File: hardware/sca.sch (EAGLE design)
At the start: 31 parts

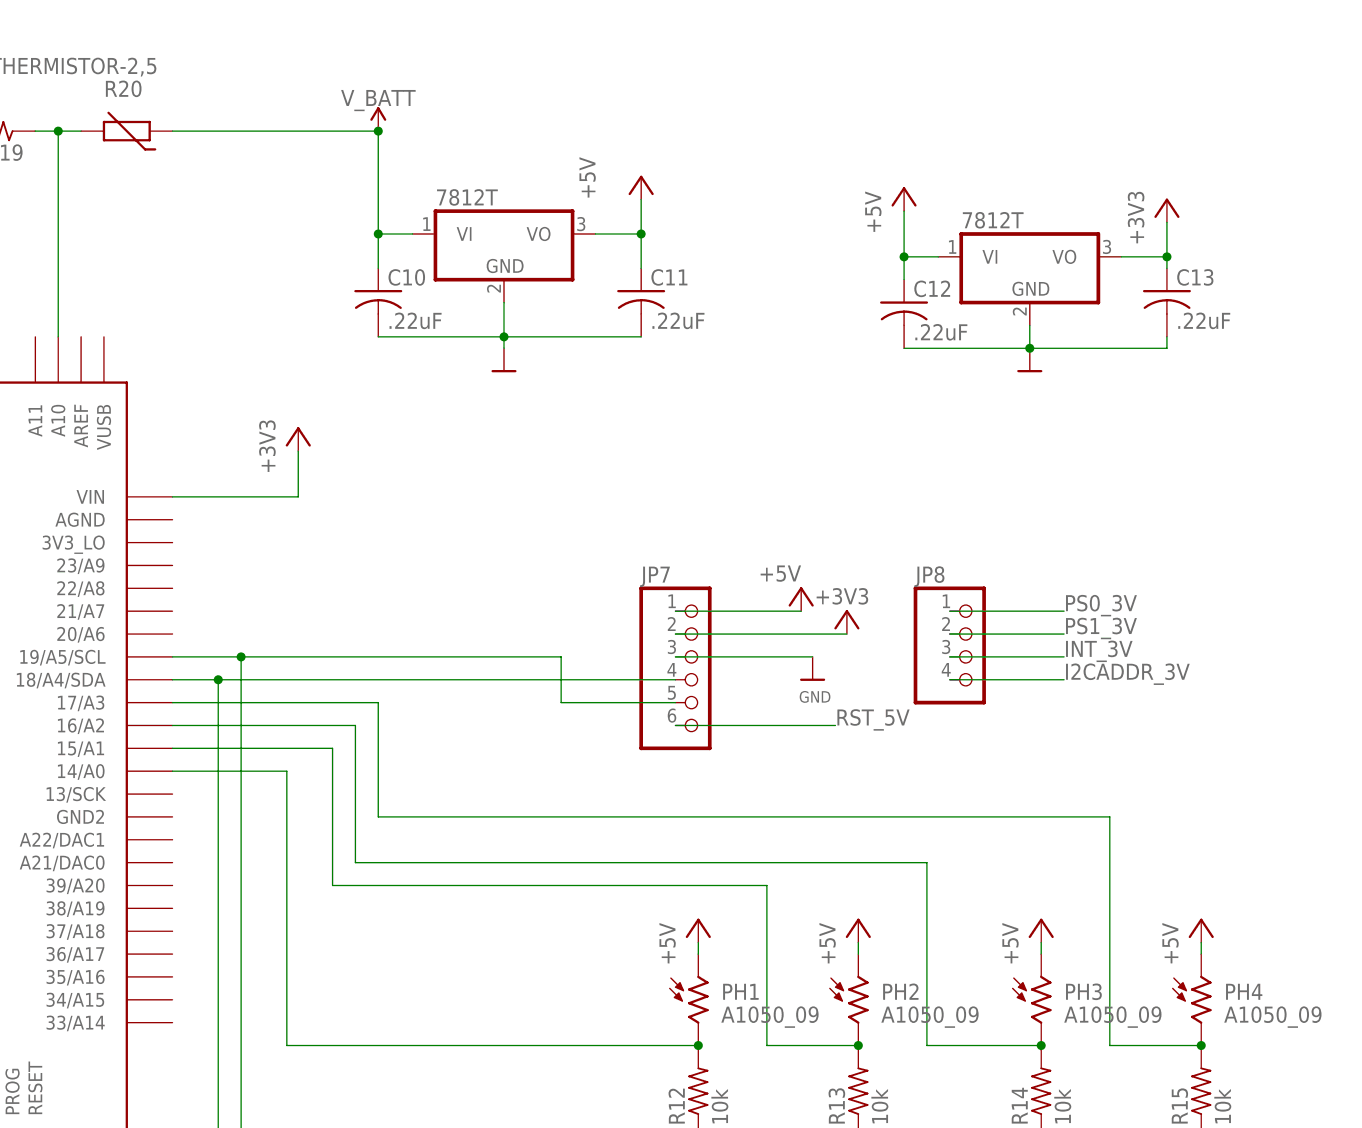
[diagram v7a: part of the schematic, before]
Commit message: made changes discussed on Sunday
temp sensor to 3V3
photoresistors to 3V3
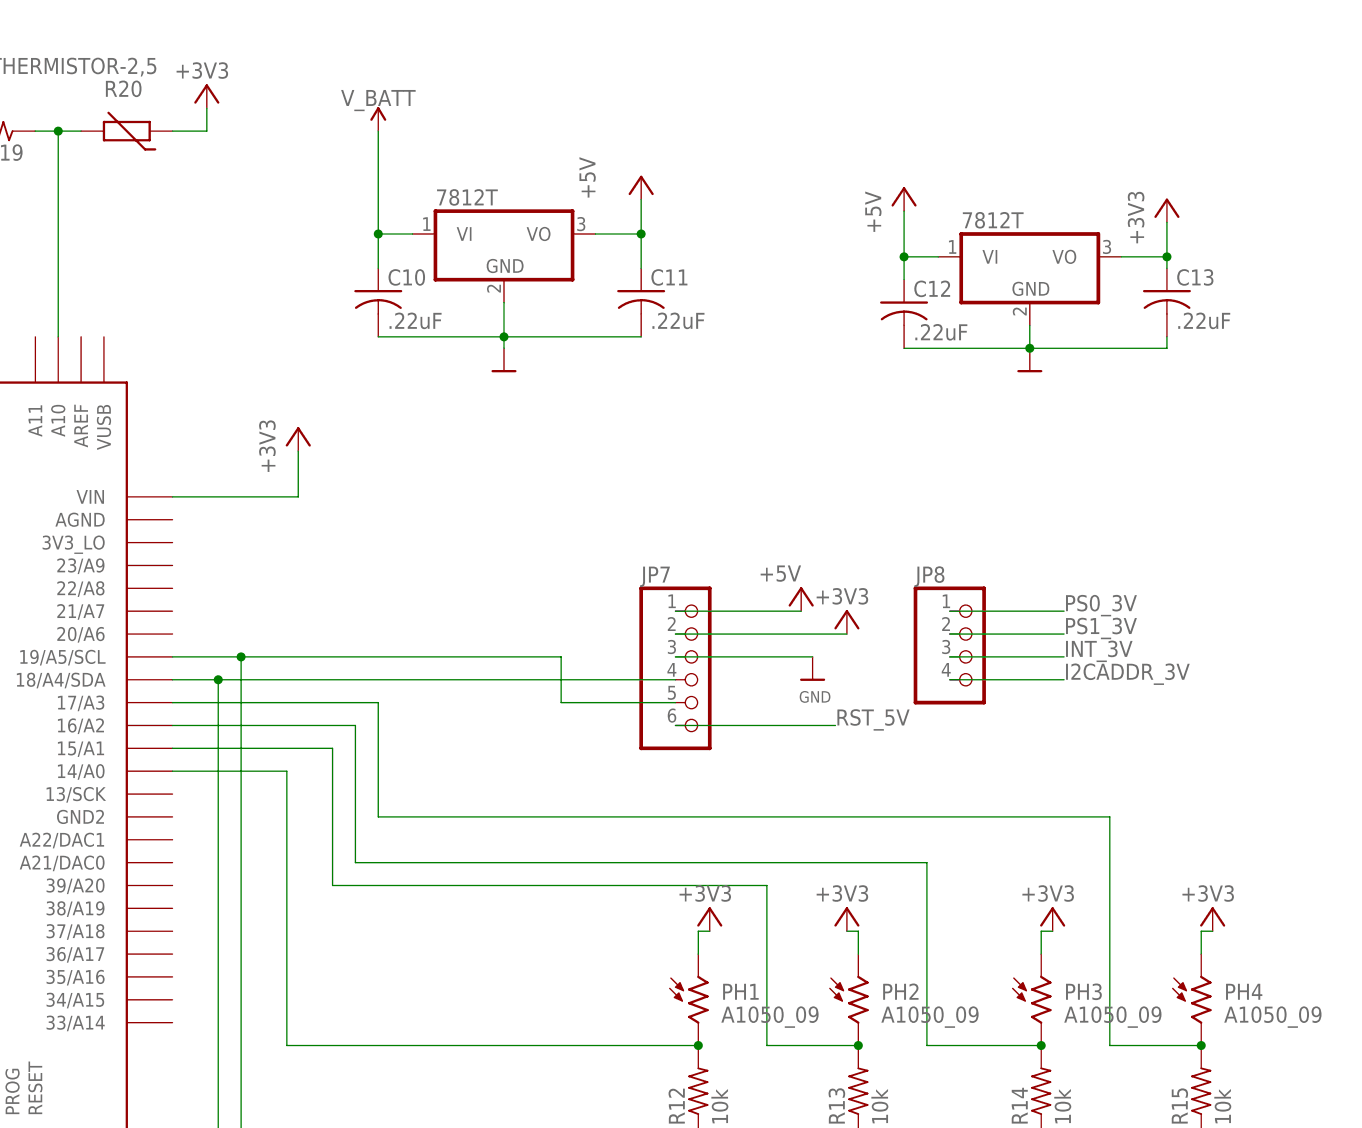
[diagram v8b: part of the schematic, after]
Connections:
- net +3V3: now also PH1.1, PH2.1, PH3.1, PH4.1, R20.1
- net +5V: no longer PH1.1, PH2.1, PH3.1, PH4.1
- net V_BATT: no longer R20.1
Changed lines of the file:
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@@
 <part name="U$28" library="microbuilder" deviceset="GND" device=""/>
 <part name="PH1" library="photo-elements" library_urn="urn:adsk.eagle:library:323" deviceset="A10" device="" package3d_urn="urn:adsk.eagle:package:22201/1" technology="50_09"/>
-<part name="P+4" library="supply1" deviceset="+5V" device=""/>
 <part name="R12" library="adafruit" library_urn="urn:adsk.eagle:library:420" deviceset="R-US_" device="0204/2V" package3d_urn="urn:adsk.eagle:package:6240630/1" value="10k"/>
 <part name="U$30" library="microbuilder" deviceset="GND" device=""/>
 <part name="PH2" library="photo-elements" library_urn="urn:adsk.eagle:library:323" deviceset="A10" device="" package3d_urn="urn:adsk.eagle:package:22201/1" technology="50_09"/>
-<part name="P+5" library="supply1" deviceset="+5V" device=""/>
 <part name="R13" library="adafruit" library_urn="urn:adsk.eagle:library:420" deviceset="R-US_" device="0204/2V" package3d_urn="urn:adsk.eagle:package:6240630/1" value="10k"/>
 <part name="U$31" library="microbuilder" deviceset="GND" device=""/>
 <part name="PH3" library="photo-elements" library_urn="urn:adsk.eagle:library:323" deviceset="A10" device="" package3d_urn="urn:adsk.eagle:package:22201/1" technology="50_09"/>
-<part name="P+6" library="supply1" deviceset="+5V" device=""/>
 <part name="R14" library="adafruit" library_urn="urn:adsk.eagle:library:420" deviceset="R-US_" device="0204/2V" package3d_urn="urn:adsk.eagle:package:6240630/1" value="10k"/>
 <part name="U$32" library="microbuilder" deviceset="GND" device=""/>
 <part name="PH4" library="photo-elements" library_urn="urn:adsk.eagle:library:323" deviceset="A10" device="" package3d_urn="urn:adsk.eagle:package:22201/1" technology="50_09"/>
-<part name="P+7" library="supply1" deviceset="+5V" device=""/>
 <part name="R15" library="adafruit" library_urn="urn:adsk.eagle:library:420" deviceset="R-US_" device="0204/2V" package3d_urn="urn:adsk.eagle:package:6240630/1" value="10k"/>
 <part name="U$33" library="microbuilder" deviceset="GND" device=""/>
@@
 <part name="SUPPLY3" library="SparkFun-PowerSymbols" library_urn="urn:adsk.eagle:library:530" deviceset="V_BATT" device=""/>
 <part name="U$8" library="microbuilder" deviceset="GND" device=""/>
+<part name="+3V5" library="supply1" deviceset="+3V3" device=""/>
+<part name="+3V7" library="supply1" deviceset="+3V3" device=""/>
+<part name="+3V8" library="supply1" deviceset="+3V3" device=""/>
+<part name="+3V9" library="supply1" deviceset="+3V3" device=""/>
+<part name="+3V10" library="supply1" deviceset="+3V3" device=""/>
 </parts>
 <sheets>
@@
 <attribute name="VALUE" x="182.88" y="60.96" size="1.778" layer="96"/>
 </instance>
-<instance part="P+4" gate="1" x="180.34" y="72.39" smashed="yes" grouprefs="PHOTORESISTORS">
-<attribute name="VALUE" x="177.8" y="67.31" size="1.778" layer="96" rot="R90"/>
-</instance>
 <instance part="R12" gate="G$1" x="180.34" y="53.34" smashed="yes" rot="R90" grouprefs="PHOTORESISTORS">
 <attribute name="NAME" x="178.8414" y="49.53" size="1.778" layer="95" rot="R90"/>
@@
 <attribute name="VALUE" x="200.66" y="60.96" size="1.778" layer="96"/>
 </instance>
-<instance part="P+5" gate="1" x="198.12" y="72.39" smashed="yes" grouprefs="PHOTORESISTORS">
-<attribute name="VALUE" x="195.58" y="67.31" size="1.778" layer="96" rot="R90"/>
-</instance>
 <instance part="R13" gate="G$1" x="198.12" y="53.34" smashed="yes" rot="R90" grouprefs="PHOTORESISTORS">
 <attribute name="NAME" x="196.6214" y="49.53" size="1.778" layer="95" rot="R90"/>
@@
 <attribute name="VALUE" x="220.98" y="60.96" size="1.778" layer="96"/>
 </instance>
-<instance part="P+6" gate="1" x="218.44" y="72.39" smashed="yes" grouprefs="PHOTORESISTORS">
-<attribute name="VALUE" x="215.9" y="67.31" size="1.778" layer="96" rot="R90"/>
-</instance>
 <instance part="R14" gate="G$1" x="218.44" y="53.34" smashed="yes" rot="R90" grouprefs="PHOTORESISTORS">
 <attribute name="NAME" x="216.9414" y="49.53" size="1.778" layer="95" rot="R90"/>
@@
 <attribute name="NAME" x="238.76" y="63.5" size="1.778" layer="95"/>
 <attribute name="VALUE" x="238.76" y="60.96" size="1.778" layer="96"/>
-</instance>
-<instance part="P+7" gate="1" x="236.22" y="72.39" smashed="yes" grouprefs="PHOTORESISTORS">
-<attribute name="VALUE" x="233.68" y="67.31" size="1.778" layer="96" rot="R90"/>
 </instance>
 <instance part="R15" gate="G$1" x="236.22" y="53.34" smashed="yes" rot="R90" grouprefs="PHOTORESISTORS">
@@
 <instance part="U$8" gate="G$1" x="36.83" y="151.13" smashed="yes">
 <attribute name="VALUE" x="35.306" y="148.59" size="1.27" layer="96"/>
+</instance>
+<instance part="+3V5" gate="G$1" x="181.61" y="73.66" smashed="yes">
+<attribute name="VALUE" x="184.15" y="76.2" size="1.778" layer="96" rot="R180"/>
+</instance>
+<instance part="+3V7" gate="G$1" x="196.85" y="73.66" smashed="yes">
+<attribute name="VALUE" x="199.39" y="76.2" size="1.778" layer="96" rot="R180"/>
+</instance>
+<instance part="+3V8" gate="G$1" x="219.71" y="73.66" smashed="yes">
+<attribute name="VALUE" x="222.25" y="76.2" size="1.778" layer="96" rot="R180"/>
+</instance>
+<instance part="+3V9" gate="G$1" x="237.49" y="73.66" smashed="yes">
+<attribute name="VALUE" x="240.03" y="76.2" size="1.778" layer="96" rot="R180"/>
+</instance>
+<instance part="+3V10" gate="G$1" x="125.73" y="165.1" smashed="yes">
+<attribute name="VALUE" x="128.27" y="167.64" size="1.778" layer="96" rot="R180"/>
 </instance>
 </instances>
@@
 <wire x1="130.81" y1="35.56" x2="130.81" y2="30.48" width="0.1524" layer="91" grouprefs="BMP338"/>
 </segment>
+<segment>
+<pinref part="PH1" gate="G$1" pin="1"/>
+<pinref part="+3V5" gate="G$1" pin="+3V3"/>
+<wire x1="180.34" y1="68.58" x2="180.34" y2="71.12" width="0.1524" layer="91"/>
+<wire x1="180.34" y1="71.12" x2="181.61" y2="71.12" width="0.1524" layer="91"/>
+</segment>
+<segment>
+<pinref part="PH2" gate="G$1" pin="1"/>
+<pinref part="+3V7" gate="G$1" pin="+3V3"/>
+<wire x1="198.12" y1="68.58" x2="198.12" y2="71.12" width="0.1524" layer="91"/>
+<wire x1="198.12" y1="71.12" x2="196.85" y2="71.12" width="0.1524" layer="91"/>
+</segment>
+<segment>
+<pinref part="+3V8" gate="G$1" pin="+3V3"/>
+<wire x1="218.44" y1="71.12" x2="219.71" y2="71.12" width="0.1524" layer="91"/>
+<pinref part="PH3" gate="G$1" pin="1"/>
+<wire x1="218.44" y1="68.58" x2="218.44" y2="71.12" width="0.1524" layer="91"/>
+</segment>
+<segment>
+<pinref part="PH4" gate="G$1" pin="1"/>
+<pinref part="+3V9" gate="G$1" pin="+3V3"/>
+<wire x1="236.22" y1="68.58" x2="236.22" y2="71.12" width="0.1524" layer="91"/>
+<wire x1="236.22" y1="71.12" x2="237.49" y2="71.12" width="0.1524" layer="91"/>
+</segment>
+<segment>
+<pinref part="R20" gate="G$1" pin="1"/>
+<wire x1="121.92" y1="160.02" x2="125.73" y2="160.02" width="0.1524" layer="91"/>
+<pinref part="+3V10" gate="G$1" pin="+3V3"/>
+<wire x1="125.73" y1="160.02" x2="125.73" y2="162.56" width="0.1524" layer="91"/>
+</segment>
 </net>
 <net name="+5V" class="0">
@@
 </segment>
 <segment>
-<pinref part="PH1" gate="G$1" pin="1"/>
-<pinref part="P+4" gate="1" pin="+5V"/>
-<wire x1="180.34" y1="68.58" x2="180.34" y2="69.85" width="0.1524" layer="91" grouprefs="PHOTORESISTORS"/>
-</segment>
-<segment>
-<pinref part="PH2" gate="G$1" pin="1"/>
-<pinref part="P+5" gate="1" pin="+5V"/>
-<wire x1="198.12" y1="68.58" x2="198.12" y2="69.85" width="0.1524" layer="91" grouprefs="PHOTORESISTORS"/>
-</segment>
-<segment>
-<pinref part="PH3" gate="G$1" pin="1"/>
-<pinref part="P+6" gate="1" pin="+5V"/>
-<wire x1="218.44" y1="68.58" x2="218.44" y2="69.85" width="0.1524" layer="91" grouprefs="PHOTORESISTORS"/>
-</segment>
-<segment>
-<pinref part="PH4" gate="G$1" pin="1"/>
-<pinref part="P+7" gate="1" pin="+5V"/>
-<wire x1="236.22" y1="68.58" x2="236.22" y2="69.85" width="0.1524" layer="91" grouprefs="PHOTORESISTORS"/>
-</segment>
-<segment>
 <pinref part="JP7" gate="A" pin="1"/>
 <pinref part="P+9" gate="1" pin="+5V"/>
@@
 <wire x1="144.78" y1="160.02" x2="144.78" y2="148.59" width="0.1524" layer="91" grouprefs="5V_REGULATOR"/>
 <junction x="144.78" y="148.59" grouprefs="5V_REGULATOR"/>
-<wire x1="144.78" y1="160.02" x2="121.92" y2="160.02" width="0.1524" layer="91"/>
-<junction x="144.78" y="160.02"/>
-<pinref part="R20" gate="G$1" pin="1"/>
-</segment>
-<segment>
+</segment>
+<segment>
